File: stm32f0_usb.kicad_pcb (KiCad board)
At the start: 2 copper layers, 41 parts, among them J1 USB_B_Mini, J2 Conn_ARM_JTAG_SWD_10, J3 Conn_01x14_Male, J4 Conn_01x14_Male, SW1 B3S-1000P, SW2 B3S-1000P, U1 STM32F042K6Tx, U2 ADP121-AUJZ33R7, U3 USBLC6-2SC6, X1 ASV-8.000MHz

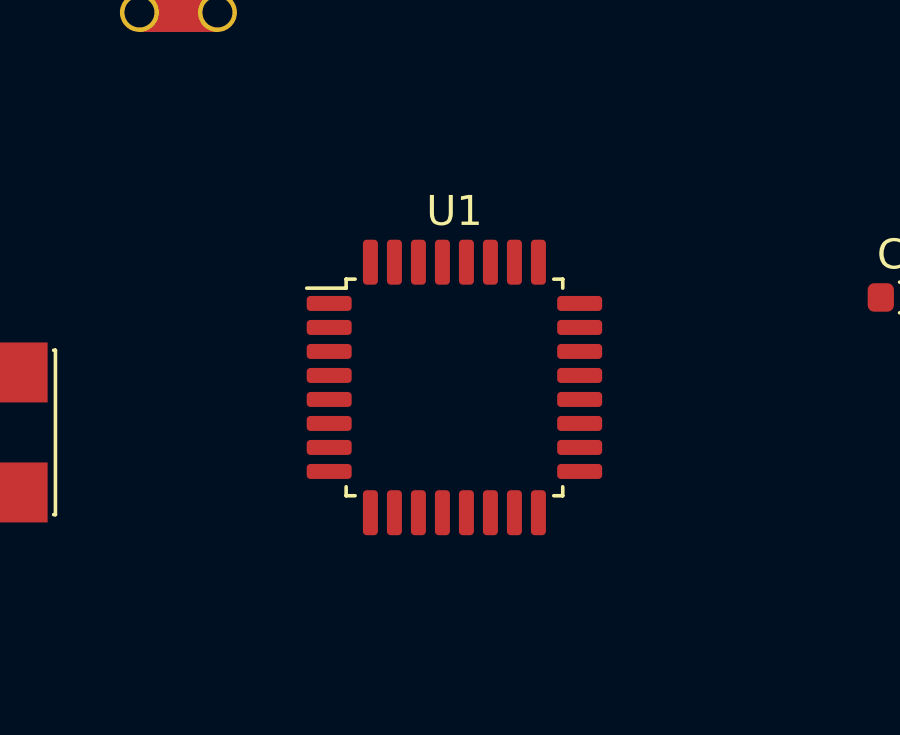
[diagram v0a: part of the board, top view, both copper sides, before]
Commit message: update GPIO/header pinout to ease routing
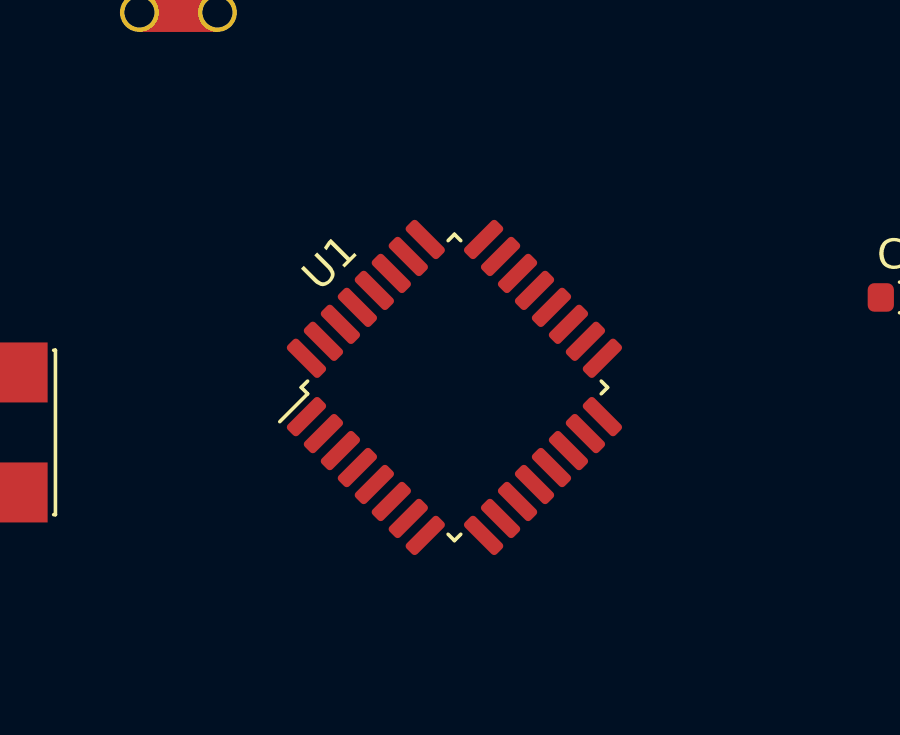
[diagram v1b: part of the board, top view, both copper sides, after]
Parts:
- turned U1 to 45 degrees
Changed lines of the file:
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@@
   )
   (module Package_QFP:LQFP-32_7x7mm_P0.8mm (layer F.Cu)
-    (at 146 91.5)
+    (at 146 91.5 45)
     (descr "LQFP, 32 Pin (https://www.nxp.com/docs/en/package-information/SOT358-1.pdf), generated with kicad-footprint-generator ipc_gullwing_generator.py")
     (tags "LQFP QFP")
     (attr smd)
-    (fp_text reference U1 (at 0 -5.88) (layer F.SilkS)
+    (fp_text reference U1 (at 0 -5.88 45) (layer F.SilkS)
       (effects (font (size 1 1) (thickness 0.15)))
     )
-    (fp_text value STM32F042K6Tx (at 0 5.88) (layer F.Fab)
+    (fp_text value STM32F042K6Tx (at 0 5.88 45) (layer F.Fab)
       (effects (font (size 1 1) (thickness 0.15)))
     )
-    (fp_text user %R (at 0 0) (layer F.Fab)
+    (fp_text user %R (at 0 0 45) (layer F.Fab)
       (effects (font (size 1 1) (thickness 0.15)))
     )
@@
     (fp_line (start 3.61 3.61) (end 3.61 3.31) (layer F.SilkS) (width 0.12))
     (fp_line (start 3.31 3.61) (end 3.61 3.61) (layer F.SilkS) (width 0.12))
-    (pad 32 smd roundrect (at -2.8 -4.175) (size 0.5 1.5) (layers F.Cu F.Paste F.Mask) (roundrect_rratio 0.25)
+    (pad 32 smd roundrect (at -2.8 -4.175 45) (size 0.5 1.5) (layers F.Cu F.Paste F.Mask) (roundrect_rratio 0.25)
       (net 1 GND))
-    (pad 31 smd roundrect (at -2 -4.175) (size 0.5 1.5) (layers F.Cu F.Paste F.Mask) (roundrect_rratio 0.25)
+    (pad 31 smd roundrect (at -2 -4.175 45) (size 0.5 1.5) (layers F.Cu F.Paste F.Mask) (roundrect_rratio 0.25)
       (net 42 /STM32/BOOT0))
-    (pad 30 smd roundrect (at -1.2 -4.175) (size 0.5 1.5) (layers F.Cu F.Paste F.Mask) (roundrect_rratio 0.25)
+    (pad 30 smd roundrect (at -1.2 -4.175 45) (size 0.5 1.5) (layers F.Cu F.Paste F.Mask) (roundrect_rratio 0.25)
       (net 33 /STM32/PB7))
-    (pad 29 smd roundrect (at -0.4 -4.175) (size 0.5 1.5) (layers F.Cu F.Paste F.Mask) (roundrect_rratio 0.25)
+    (pad 29 smd roundrect (at -0.4 -4.175 45) (size 0.5 1.5) (layers F.Cu F.Paste F.Mask) (roundrect_rratio 0.25)
       (net 34 /STM32/PB6))
-    (pad 28 smd roundrect (at 0.4 -4.175) (size 0.5 1.5) (layers F.Cu F.Paste F.Mask) (roundrect_rratio 0.25)
+    (pad 28 smd roundrect (at 0.4 -4.175 45) (size 0.5 1.5) (layers F.Cu F.Paste F.Mask) (roundrect_rratio 0.25)
       (net 35 /STM32/PB5))
-    (pad 27 smd roundrect (at 1.2 -4.175) (size 0.5 1.5) (layers F.Cu F.Paste F.Mask) (roundrect_rratio 0.25)
+    (pad 27 smd roundrect (at 1.2 -4.175 45) (size 0.5 1.5) (layers F.Cu F.Paste F.Mask) (roundrect_rratio 0.25)
       (net 36 /STM32/PB4))
-    (pad 26 smd roundrect (at 2 -4.175) (size 0.5 1.5) (layers F.Cu F.Paste F.Mask) (roundrect_rratio 0.25)
+    (pad 26 smd roundrect (at 2 -4.175 45) (size 0.5 1.5) (layers F.Cu F.Paste F.Mask) (roundrect_rratio 0.25)
       (net 37 /STM32/PB3))
-    (pad 25 smd roundrect (at 2.8 -4.175) (size 0.5 1.5) (layers F.Cu F.Paste F.Mask) (roundrect_rratio 0.25)
+    (pad 25 smd roundrect (at 2.8 -4.175 45) (size 0.5 1.5) (layers F.Cu F.Paste F.Mask) (roundrect_rratio 0.25)
       (net 40 /STM32/PA15))
-    (pad 24 smd roundrect (at 4.175 -2.8) (size 1.5 0.5) (layers F.Cu F.Paste F.Mask) (roundrect_rratio 0.25)
+    (pad 24 smd roundrect (at 4.175 -2.8 45) (size 1.5 0.5) (layers F.Cu F.Paste F.Mask) (roundrect_rratio 0.25)
       (net 20 /STM32/PA14_SWCLK))
-    (pad 23 smd roundrect (at 4.175 -2) (size 1.5 0.5) (layers F.Cu F.Paste F.Mask) (roundrect_rratio 0.25)
+    (pad 23 smd roundrect (at 4.175 -2 45) (size 1.5 0.5) (layers F.Cu F.Paste F.Mask) (roundrect_rratio 0.25)
       (net 21 /STM32/PA13_SWDIO))
-    (pad 22 smd roundrect (at 4.175 -1.2) (size 1.5 0.5) (layers F.Cu F.Paste F.Mask) (roundrect_rratio 0.25)
+    (pad 22 smd roundrect (at 4.175 -1.2 45) (size 1.5 0.5) (layers F.Cu F.Paste F.Mask) (roundrect_rratio 0.25)
       (net 43 /STM32/USB_DP))
-    (pad 21 smd roundrect (at 4.175 -0.4) (size 1.5 0.5) (layers F.Cu F.Paste F.Mask) (roundrect_rratio 0.25)
+    (pad 21 smd roundrect (at 4.175 -0.4 45) (size 1.5 0.5) (layers F.Cu F.Paste F.Mask) (roundrect_rratio 0.25)
       (net 44 /STM32/USB_DM))
-    (pad 20 smd roundrect (at 4.175 0.4) (size 1.5 0.5) (layers F.Cu F.Paste F.Mask) (roundrect_rratio 0.25)
+    (pad 20 smd roundrect (at 4.175 0.4 45) (size 1.5 0.5) (layers F.Cu F.Paste F.Mask) (roundrect_rratio 0.25)
       (net 22 /STM32/PA10))
-    (pad 19 smd roundrect (at 4.175 1.2) (size 1.5 0.5) (layers F.Cu F.Paste F.Mask) (roundrect_rratio 0.25)
+    (pad 19 smd roundrect (at 4.175 1.2 45) (size 1.5 0.5) (layers F.Cu F.Paste F.Mask) (roundrect_rratio 0.25)
       (net 23 /STM32/PA9))
-    (pad 18 smd roundrect (at 4.175 2) (size 1.5 0.5) (layers F.Cu F.Paste F.Mask) (roundrect_rratio 0.25)
+    (pad 18 smd roundrect (at 4.175 2 45) (size 1.5 0.5) (layers F.Cu F.Paste F.Mask) (roundrect_rratio 0.25)
       (net 24 /STM32/PA8))
-    (pad 17 smd roundrect (at 4.175 2.8) (size 1.5 0.5) (layers F.Cu F.Paste F.Mask) (roundrect_rratio 0.25)
+    (pad 17 smd roundrect (at 4.175 2.8 45) (size 1.5 0.5) (layers F.Cu F.Paste F.Mask) (roundrect_rratio 0.25)
       (net 8 VDD))
-    (pad 16 smd roundrect (at 2.8 4.175) (size 0.5 1.5) (layers F.Cu F.Paste F.Mask) (roundrect_rratio 0.25)
+    (pad 16 smd roundrect (at 2.8 4.175 45) (size 0.5 1.5) (layers F.Cu F.Paste F.Mask) (roundrect_rratio 0.25)
       (net 1 GND))
-    (pad 15 smd roundrect (at 2 4.175) (size 0.5 1.5) (layers F.Cu F.Paste F.Mask) (roundrect_rratio 0.25)
+    (pad 15 smd roundrect (at 2 4.175 45) (size 0.5 1.5) (layers F.Cu F.Paste F.Mask) (roundrect_rratio 0.25)
       (net 38 /STM32/PB1))
-    (pad 14 smd roundrect (at 1.2 4.175) (size 0.5 1.5) (layers F.Cu F.Paste F.Mask) (roundrect_rratio 0.25)
+    (pad 14 smd roundrect (at 1.2 4.175 45) (size 0.5 1.5) (layers F.Cu F.Paste F.Mask) (roundrect_rratio 0.25)
       (net 39 /STM32/PB0))
-    (pad 13 smd roundrect (at 0.4 4.175) (size 0.5 1.5) (layers F.Cu F.Paste F.Mask) (roundrect_rratio 0.25)
+    (pad 13 smd roundrect (at 0.4 4.175 45) (size 0.5 1.5) (layers F.Cu F.Paste F.Mask) (roundrect_rratio 0.25)
       (net 25 /STM32/PA7))
-    (pad 12 smd roundrect (at -0.4 4.175) (size 0.5 1.5) (layers F.Cu F.Paste F.Mask) (roundrect_rratio 0.25)
+    (pad 12 smd roundrect (at -0.4 4.175 45) (size 0.5 1.5) (layers F.Cu F.Paste F.Mask) (roundrect_rratio 0.25)
       (net 26 /STM32/PA6))
-    (pad 11 smd roundrect (at -1.2 4.175) (size 0.5 1.5) (layers F.Cu F.Paste F.Mask) (roundrect_rratio 0.25)
+    (pad 11 smd roundrect (at -1.2 4.175 45) (size 0.5 1.5) (layers F.Cu F.Paste F.Mask) (roundrect_rratio 0.25)
       (net 27 /STM32/PA5))
-    (pad 10 smd roundrect (at -2 4.175) (size 0.5 1.5) (layers F.Cu F.Paste F.Mask) (roundrect_rratio 0.25)
+    (pad 10 smd roundrect (at -2 4.175 45) (size 0.5 1.5) (layers F.Cu F.Paste F.Mask) (roundrect_rratio 0.25)
       (net 28 /STM32/PA4))
-    (pad 9 smd roundrect (at -2.8 4.175) (size 0.5 1.5) (layers F.Cu F.Paste F.Mask) (roundrect_rratio 0.25)
+    (pad 9 smd roundrect (at -2.8 4.175 45) (size 0.5 1.5) (layers F.Cu F.Paste F.Mask) (roundrect_rratio 0.25)
       (net 29 /STM32/PA3))
-    (pad 8 smd roundrect (at -4.175 2.8) (size 1.5 0.5) (layers F.Cu F.Paste F.Mask) (roundrect_rratio 0.25)
+    (pad 8 smd roundrect (at -4.175 2.8 45) (size 1.5 0.5) (layers F.Cu F.Paste F.Mask) (roundrect_rratio 0.25)
       (net 30 /STM32/PA2))
-    (pad 7 smd roundrect (at -4.175 2) (size 1.5 0.5) (layers F.Cu F.Paste F.Mask) (roundrect_rratio 0.25)
+    (pad 7 smd roundrect (at -4.175 2 45) (size 1.5 0.5) (layers F.Cu F.Paste F.Mask) (roundrect_rratio 0.25)
       (net 31 /STM32/PA1))
-    (pad 6 smd roundrect (at -4.175 1.2) (size 1.5 0.5) (layers F.Cu F.Paste F.Mask) (roundrect_rratio 0.25)
+    (pad 6 smd roundrect (at -4.175 1.2 45) (size 1.5 0.5) (layers F.Cu F.Paste F.Mask) (roundrect_rratio 0.25)
       (net 11 /STM32/PA0))
-    (pad 5 smd roundrect (at -4.175 0.4) (size 1.5 0.5) (layers F.Cu F.Paste F.Mask) (roundrect_rratio 0.25)
+    (pad 5 smd roundrect (at -4.175 0.4 45) (size 1.5 0.5) (layers F.Cu F.Paste F.Mask) (roundrect_rratio 0.25)
       (net 9 VDDA))
-    (pad 4 smd roundrect (at -4.175 -0.4) (size 1.5 0.5) (layers F.Cu F.Paste F.Mask) (roundrect_rratio 0.25)
+    (pad 4 smd roundrect (at -4.175 -0.4 45) (size 1.5 0.5) (layers F.Cu F.Paste F.Mask) (roundrect_rratio 0.25)
       (net 6 /STM32/NRST))
-    (pad 3 smd roundrect (at -4.175 -1.2) (size 1.5 0.5) (layers F.Cu F.Paste F.Mask) (roundrect_rratio 0.25)
+    (pad 3 smd roundrect (at -4.175 -1.2 45) (size 1.5 0.5) (layers F.Cu F.Paste F.Mask) (roundrect_rratio 0.25)
       (net 32 /STM32/PF1))
-    (pad 2 smd roundrect (at -4.175 -2) (size 1.5 0.5) (layers F.Cu F.Paste F.Mask) (roundrect_rratio 0.25)
+    (pad 2 smd roundrect (at -4.175 -2 45) (size 1.5 0.5) (layers F.Cu F.Paste F.Mask) (roundrect_rratio 0.25)
       (net 47 /STM32/clkin))
-    (pad 1 smd roundrect (at -4.175 -2.8) (size 1.5 0.5) (layers F.Cu F.Paste F.Mask) (roundrect_rratio 0.25)
+    (pad 1 smd roundrect (at -4.175 -2.8 45) (size 1.5 0.5) (layers F.Cu F.Paste F.Mask) (roundrect_rratio 0.25)
       (net 8 VDD))
     (model ${KISYS3DMOD}/Package_QFP.3dshapes/LQFP-32_7x7mm_P0.8mm.wrl
